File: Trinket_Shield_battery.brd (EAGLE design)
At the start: 15.2 x 20.3 mm, 12 parts, among them IC1 MCP73831/OT

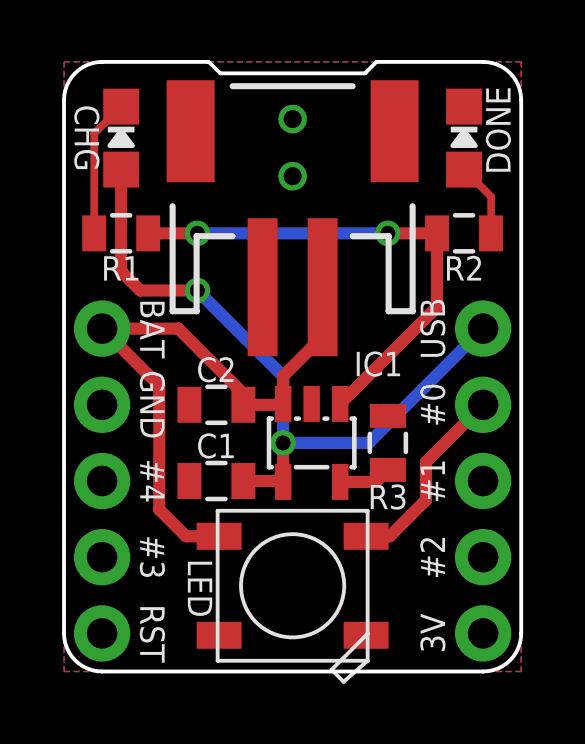
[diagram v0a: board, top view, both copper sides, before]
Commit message: Reroute LED VDD
Rerouted the VDD to the WS2812B LED - Better grounding of the
capacitors.
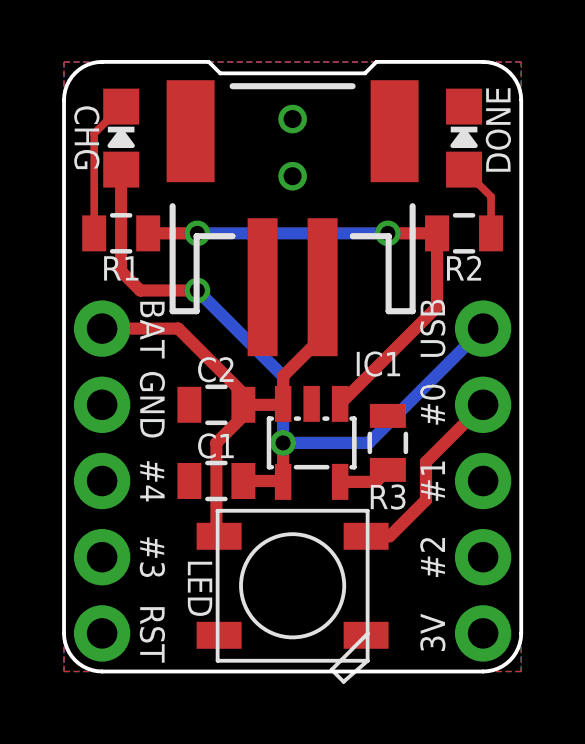
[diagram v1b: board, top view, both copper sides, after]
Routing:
- net V_BATT: track 20.9 -> 16.5 mm
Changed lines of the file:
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@@
 <layer number="23" name="tOrigins" color="15" fill="1" visible="yes" active="yes"/>
 <layer number="24" name="bOrigins" color="15" fill="1" visible="yes" active="yes"/>
-<layer number="25" name="tNames" color="9" fill="1" visible="yes" active="yes"/>
+<layer number="25" name="tNames" color="14" fill="1" visible="yes" active="yes"/>
 <layer number="26" name="bNames" color="7" fill="1" visible="yes" active="yes"/>
 <layer number="27" name="tValues" color="7" fill="1" visible="yes" active="yes"/>
@@
 <wire x1="5.98" y1="9.26" x2="3.81" y2="11.43" width="0.4064" layer="1"/>
 <wire x1="3.81" y1="11.43" x2="1.27" y2="11.43" width="0.4064" layer="1"/>
-<wire x1="3.175" y1="9.525" x2="1.27" y2="11.43" width="0.4064" layer="1"/>
-<wire x1="5.17" y1="4.5075" x2="4.065" y2="4.5075" width="0.4064" layer="1"/>
-<wire x1="4.065" y1="4.5075" x2="3.175" y2="5.3975" width="0.4064" layer="1"/>
-<wire x1="3.175" y1="5.3975" x2="3.175" y2="9.525" width="0.4064" layer="1"/>
+<wire x1="5.98" y1="8.89" x2="5.98" y2="8.52" width="0.4064" layer="1"/>
+<wire x1="5.98" y1="8.52" x2="5.08" y2="7.62" width="0.4064" layer="1"/>
+<wire x1="5.08" y1="7.62" x2="5.08" y2="4.5975" width="0.4064" layer="1"/>
+<wire x1="5.08" y1="4.5975" x2="5.17" y2="4.5075" width="0.4064" layer="1"/>
 </signal>
 <signal name="N$3">

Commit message: Update USB Power to CHG LED
Slight change in route of USB power to CHG LED.
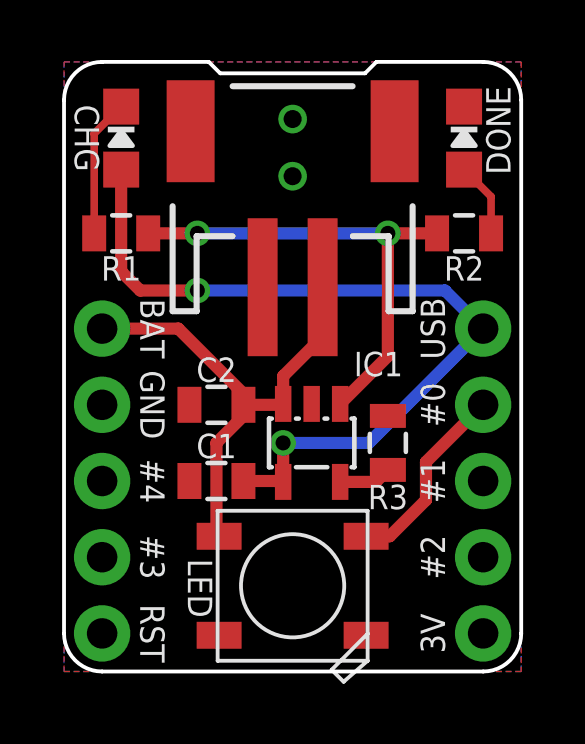
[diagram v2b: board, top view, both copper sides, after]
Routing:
- net V_USB: track 23.3 -> 27.1 mm
- net N$6: track 16.7 -> 16.0 mm
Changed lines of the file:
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@@
 <wire x1="10.16" y1="7.62" x2="7.3025" y2="7.62" width="0.4064" layer="16"/>
 <via x="4.445" y="12.7" extent="1-16" drill="0.5"/>
-<wire x1="4.445" y1="12.7" x2="7.3025" y2="9.8425" width="0.4064" layer="16"/>
-<wire x1="7.3025" y1="9.8425" x2="7.3025" y2="7.62" width="0.4064" layer="16"/>
 <wire x1="4.445" y1="12.7" x2="2.54" y2="12.7" width="0.4064" layer="1"/>
 <wire x1="2.54" y1="12.7" x2="1.905" y2="13.335" width="0.4064" layer="1"/>
@@
 <wire x1="5.98" y1="6.35" x2="7.275" y2="6.35" width="0.4064" layer="1"/>
 <wire x1="7.275" y1="6.35" x2="7.305" y2="6.32" width="0.4064" layer="1" curve="-90"/>
+<wire x1="4.445" y1="12.7" x2="12.7" y2="12.7" width="0.4064" layer="16"/>
+<wire x1="12.7" y1="12.7" x2="13.97" y2="11.43" width="0.4064" layer="16"/>
 </signal>
 <signal name="V_BATT">
@@
 <contactref element="R2" pad="1"/>
 <contactref element="IC1" pad="1"/>
-<wire x1="9.205" y1="8.92" x2="12.435" y2="12.15" width="0.4064" layer="1"/>
-<wire x1="12.435" y1="12.15" x2="12.435" y2="14.605" width="0.4064" layer="1"/>
 <wire x1="4.445" y1="14.605" x2="2.805" y2="14.605" width="0.4064" layer="1"/>
 <wire x1="12.435" y1="14.605" x2="10.795" y2="14.605" width="0.4064" layer="1"/>
@@
 <via x="10.795" y="14.605" extent="1-16" drill="0.5"/>
 <wire x1="4.445" y1="14.605" x2="10.795" y2="14.605" width="0.4064" layer="16"/>
+<wire x1="9.205" y1="8.92" x2="10.795" y2="10.51" width="0.4064" layer="1"/>
+<wire x1="10.795" y1="10.51" x2="10.795" y2="14.605" width="0.4064" layer="1"/>
 </signal>
 <signal name="N$7">

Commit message: Updated Board Silk
Added the OSHW Icon and some polarity indicators for the battery connector.
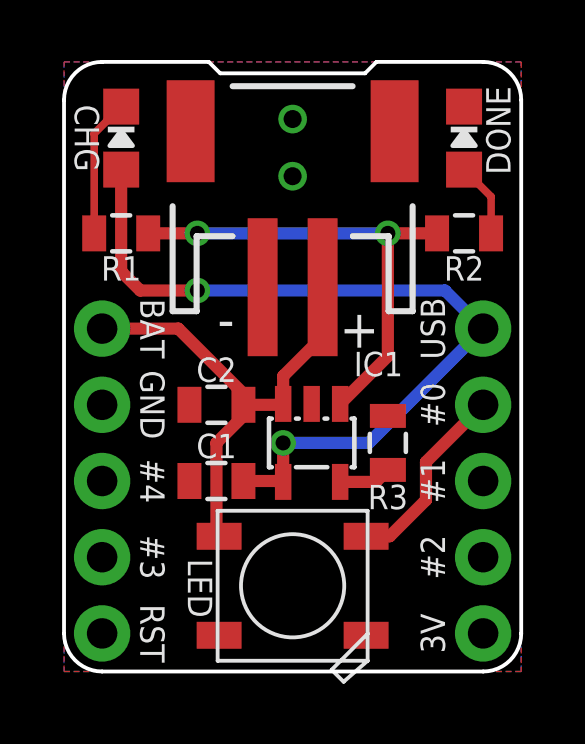
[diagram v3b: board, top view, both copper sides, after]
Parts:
- added U$1: (no value), SparkFun-Aesthetics:OSHW-LOGO-M
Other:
- board text added: "+"
- board text added: "-"
- board text added: "Trinket Battery Shield v1.01 04/28/2016"
- board text removed: "Trinket Battery Shield v1.0 04/25/2016"
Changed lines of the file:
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@@
 <text x="2.54" y="1.27" size="0.8128" layer="25" font="vector" ratio="15" rot="SR270" align="bottom-center">RST</text>
 <text x="12.7" y="1.27" size="0.8128" layer="22" font="vector" ratio="15" rot="SMR0">Trinket Battery
-Shield v1.0
-04/25/2016</text>
+Shield v1.01
+04/28/2016</text>
+<text x="9.8425" y="11.43" size="1.27" layer="21" font="vector" ratio="15" align="center">+</text>
+<text x="5.3975" y="11.43" size="1.27" layer="21" font="vector" ratio="15" rot="SR180" align="center">-</text>
 </plain>
 <attributes>
@@
 <attribute name="NAME" x="4.1275" y="2.775" size="0.8128" layer="25" font="vector" ratio="15" rot="SR270" align="bottom-center"/>
 </element>
+<element name="U$1" library="SparkFun-Aesthetics" package="OSHW-LOGO-M" value="" x="7.62" y="10.16" rot="MR0"/>
 </elements>
 <signals>
